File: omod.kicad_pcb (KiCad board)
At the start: 2 copper layers, 147.3 x 97.8 mm, 28 parts, among them P1 Motor_control, P2 Motor_1, P3 Motor_2, Q1 Q_NPN_BCE, Q2 IRF540N, Q3 Q_NPN_BCE, Q4 IRF540N, U1 LM7810ACT

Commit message: ok simulation and removed TVS
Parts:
- removed D5, D7, D9: TVS_30, Diodes_ThroughHole:Diode_DO-35_SOD27_Horizontal_RM10
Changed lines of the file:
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@@
-(kicad_pcb (version 4) (host pcbnew 4.0.3-stable)
+(kicad_pcb (version 4) (host pcbnew 4.0.6)
   (general
-    (links 59)
+    (links 53)
     (no_connects 0)
     (area 12.649999 11.270001 221.209999 110.540001)
@@
     (tracks 250)
     (zones 0)
-    (modules 28)
+    (modules 25)
     (nets 26)
   )
@@
     (pad_to_mask_clearance 0)
     (aux_axis_origin 0 0)
-    (visible_elements 7FFFFFFF)
+    (visible_elements 7FFFEFFF)
     (pcbplotparams
       (layerselection 0x00030_80000001)
@@
   )
   (module Diodes_ThroughHole:Diode_DO-35_SOD27_Horizontal_RM10 placed (layer F.Cu)
-    (at 58.42 73.66 270)
-    (descr "Diode, DO-35,  SOD27, Horizontal, RM 10mm")
-    (tags "Diode, DO-35, SOD27, Horizontal, RM 10mm, 1N4148,")
-    (fp_text reference D5 (at 5.43052 2.53746 270) (layer F.SilkS)
-      (effects (font (size 1 1) (thickness 0.15)))
-    )
-    (fp_text value TVS_30 (at 4.41452 -3.55854 270) (layer F.Fab)
-      (effects (font (size 1 1) (thickness 0.15)))
-    )
-    (fp_line (start 7.36652 -0.00254) (end 8.76352 -0.00254) (layer F.SilkS) (width 0.15))
-    (fp_line (start 2.92152 -0.00254) (end 1.39752 -0.00254) (layer F.SilkS) (width 0.15))
-    (fp_line (start 3.30252 -0.76454) (end 3.30252 0.75946) (layer F.SilkS) (width 0.15))
-    (fp_line (start 3.04852 -0.76454) (end 3.04852 0.75946) (layer F.SilkS) (width 0.15))
-    (fp_line (start 2.79452 -0.00254) (end 2.79452 0.75946) (layer F.SilkS) (width 0.15))
-    (fp_line (start 2.79452 0.75946) (end 7.36652 0.75946) (layer F.SilkS) (width 0.15))
-    (fp_line (start 7.36652 0.75946) (end 7.36652 -0.76454) (layer F.SilkS) (width 0.15))
-    (fp_line (start 7.36652 -0.76454) (end 2.79452 -0.76454) (layer F.SilkS) (width 0.15))
-    (fp_line (start 2.79452 -0.76454) (end 2.79452 -0.00254) (layer F.SilkS) (width 0.15))
-    (pad 2 thru_hole circle (at 10.16052 -0.00254 90) (size 1.69926 1.69926) (drill 0.70104) (layers *.Cu *.Mask F.SilkS)
-      (net 1 GND))
-    (pad 1 thru_hole rect (at 0.00052 -0.00254 90) (size 1.69926 1.69926) (drill 0.70104) (layers *.Cu *.Mask F.SilkS)
-      (net 4 "Net-(D4-Pad1)"))
-    (model Diodes_ThroughHole.3dshapes/Diode_DO-35_SOD27_Horizontal_RM10.wrl
-      (at (xyz 0.2 0 0))
-      (scale (xyz 0.4 0.4 0.4))
-      (rotate (xyz 0 0 180))
-    )
-  )
-  (module Diodes_ThroughHole:Diode_DO-35_SOD27_Horizontal_RM10 placed (layer F.Cu)
     (at 138.43 52.07)
     (descr "Diode, DO-35,  SOD27, Horizontal, RM 10mm")
@@
   )
   (module Diodes_ThroughHole:Diode_DO-35_SOD27_Horizontal_RM10 placed (layer F.Cu)
-    (at 110.49 81.28 180)
-    (descr "Diode, DO-35,  SOD27, Horizontal, RM 10mm")
-    (tags "Diode, DO-35, SOD27, Horizontal, RM 10mm, 1N4148,")
-    (fp_text reference D7 (at 5.43052 2.53746 180) (layer F.SilkS)
-      (effects (font (size 1 1) (thickness 0.15)))
-    )
-    (fp_text value TVS_30 (at 4.41452 -3.55854 180) (layer F.Fab)
-      (effects (font (size 1 1) (thickness 0.15)))
-    )
-    (fp_line (start 7.36652 -0.00254) (end 8.76352 -0.00254) (layer F.SilkS) (width 0.15))
-    (fp_line (start 2.92152 -0.00254) (end 1.39752 -0.00254) (layer F.SilkS) (width 0.15))
-    (fp_line (start 3.30252 -0.76454) (end 3.30252 0.75946) (layer F.SilkS) (width 0.15))
-    (fp_line (start 3.04852 -0.76454) (end 3.04852 0.75946) (layer F.SilkS) (width 0.15))
-    (fp_line (start 2.79452 -0.00254) (end 2.79452 0.75946) (layer F.SilkS) (width 0.15))
-    (fp_line (start 2.79452 0.75946) (end 7.36652 0.75946) (layer F.SilkS) (width 0.15))
-    (fp_line (start 7.36652 0.75946) (end 7.36652 -0.76454) (layer F.SilkS) (width 0.15))
-    (fp_line (start 7.36652 -0.76454) (end 2.79452 -0.76454) (layer F.SilkS) (width 0.15))
-    (fp_line (start 2.79452 -0.76454) (end 2.79452 -0.00254) (layer F.SilkS) (width 0.15))
-    (pad 2 thru_hole circle (at 10.16052 -0.00254) (size 1.69926 1.69926) (drill 0.70104) (layers *.Cu *.Mask F.SilkS)
-      (net 7 "Net-(D7-Pad2)"))
-    (pad 1 thru_hole rect (at 0.00052 -0.00254) (size 1.69926 1.69926) (drill 0.70104) (layers *.Cu *.Mask F.SilkS)
-      (net 8 "Net-(D7-Pad1)"))
-    (model Diodes_ThroughHole.3dshapes/Diode_DO-35_SOD27_Horizontal_RM10.wrl
-      (at (xyz 0.2 0 0))
-      (scale (xyz 0.4 0.4 0.4))
-      (rotate (xyz 0 0 180))
-    )
-  )
-  (module Diodes_ThroughHole:Diode_DO-35_SOD27_Horizontal_RM10 placed (layer F.Cu)
     (at 80.01 67.31 90)
     (descr "Diode, DO-35,  SOD27, Horizontal, RM 10mm")
@@
     (pad 1 thru_hole rect (at 0.00052 -0.00254 270) (size 1.69926 1.69926) (drill 0.70104) (layers *.Cu *.Mask F.SilkS)
       (net 10 "Net-(D8-Pad1)"))
-    (model Diodes_ThroughHole.3dshapes/Diode_DO-35_SOD27_Horizontal_RM10.wrl
-      (at (xyz 0.2 0 0))
-      (scale (xyz 0.4 0.4 0.4))
-      (rotate (xyz 0 0 180))
-    )
-  )
-  (module Diodes_ThroughHole:Diode_DO-35_SOD27_Horizontal_RM10 placed (layer F.Cu)
-    (at 49.53 78.74 180)
-    (descr "Diode, DO-35,  SOD27, Horizontal, RM 10mm")
-    (tags "Diode, DO-35, SOD27, Horizontal, RM 10mm, 1N4148,")
-    (fp_text reference D9 (at 5.43052 2.53746 180) (layer F.SilkS)
-      (effects (font (size 1 1) (thickness 0.15)))
-    )
-    (fp_text value TVS_30 (at 4.41452 -3.55854 180) (layer F.Fab)
-      (effects (font (size 1 1) (thickness 0.15)))
-    )
-    (fp_line (start 7.36652 -0.00254) (end 8.76352 -0.00254) (layer F.SilkS) (width 0.15))
-    (fp_line (start 2.92152 -0.00254) (end 1.39752 -0.00254) (layer F.SilkS) (width 0.15))
-    (fp_line (start 3.30252 -0.76454) (end 3.30252 0.75946) (layer F.SilkS) (width 0.15))
-    (fp_line (start 3.04852 -0.76454) (end 3.04852 0.75946) (layer F.SilkS) (width 0.15))
-    (fp_line (start 2.79452 -0.00254) (end 2.79452 0.75946) (layer F.SilkS) (width 0.15))
-    (fp_line (start 2.79452 0.75946) (end 7.36652 0.75946) (layer F.SilkS) (width 0.15))
-    (fp_line (start 7.36652 0.75946) (end 7.36652 -0.76454) (layer F.SilkS) (width 0.15))
-    (fp_line (start 7.36652 -0.76454) (end 2.79452 -0.76454) (layer F.SilkS) (width 0.15))
-    (fp_line (start 2.79452 -0.76454) (end 2.79452 -0.00254) (layer F.SilkS) (width 0.15))
-    (pad 2 thru_hole circle (at 10.16052 -0.00254) (size 1.69926 1.69926) (drill 0.70104) (layers *.Cu *.Mask F.SilkS)
-      (net 11 "Net-(D9-Pad2)"))
-    (pad 1 thru_hole rect (at 0.00052 -0.00254) (size 1.69926 1.69926) (drill 0.70104) (layers *.Cu *.Mask F.SilkS)
-      (net 12 "Net-(D9-Pad1)"))
     (model Diodes_ThroughHole.3dshapes/Diode_DO-35_SOD27_Horizontal_RM10.wrl
       (at (xyz 0.2 0 0))
@@
   (segment (start 134.62 48.26) (end 134.62306 48.26) (width 1) (layer B.Cu) (net 6))
   (segment (start 144.78052 66.03948) (end 144.78 66.04) (width 1) (layer B.Cu) (net 6))
-  (segment (start 100.32948 81.28254) (end 100.32948 90.16948) (width 2) (layer B.Cu) (net 7) (status 400000))
-  (segment (start 100.32948 90.16948) (end 102.87 92.71) (width 2) (layer B.Cu) (net 7) (status 800000))
+  (segment (start 100.32948 81.28254) (end 100.32948 90.16948) (width 2) (layer B.Cu) (net 7))
+  (segment (start 100.32948 90.16948) (end 102.87 92.71) (width 2) (layer B.Cu) (net 7))
   (segment (start 123.19 54.61) (end 121.92 54.61) (width 2) (layer B.Cu) (net 7))
   (segment (start 104.13746 81.28254) (end 106.68 78.74) (width 2) (layer B.Cu) (net 7))
@@
   (segment (start 124.46 55.88) (end 123.19 54.61) (width 1.9) (layer B.Cu) (net 7))
   (segment (start 123.19 54.61) (end 123.19 54.61) (width 1.9) (layer B.Cu) (net 7))
-  (segment (start 110.48948 81.28254) (end 110.48948 90.09052) (width 2) (layer B.Cu) (net 8) (status 400000))
-  (segment (start 110.48948 90.09052) (end 107.87 92.71) (width 2) (layer B.Cu) (net 8) (status 800000))
+  (segment (start 110.48948 81.28254) (end 110.48948 90.09052) (width 2) (layer B.Cu) (net 8))
+  (segment (start 110.48948 90.09052) (end 107.87 92.71) (width 2) (layer B.Cu) (net 8))
   (segment (start 110.48948 81.28254) (end 110.48948 71.12052) (width 2) (layer B.Cu) (net 8))
   (segment (start 124.46 68.58) (end 124.46 66.04) (width 2) (layer B.Cu) (net 8))
@@
   (segment (start 53.34 57.15) (end 50.8 54.61) (width 2) (layer B.Cu) (net 11))
   (segment (start 53.34 58.42) (end 53.34 57.15) (width 2) (layer B.Cu) (net 11))
-  (segment (start 53.34 66.04) (end 53.34 74.93202) (width 2) (layer B.Cu) (net 12) (status 400000))
-  (segment (start 53.34 74.93202) (end 49.52948 78.74254) (width 2) (layer B.Cu) (net 12) (status 800000))
+  (segment (start 53.34 66.04) (end 53.34 74.93202) (width 2) (layer B.Cu) (net 12))
+  (segment (start 53.34 74.93202) (end 49.52948 78.74254) (width 2) (layer B.Cu) (net 12))
   (segment (start 44.37 92.71) (end 44.37 83.90202) (width 2) (layer B.Cu) (net 12))
   (segment (start 44.37 83.90202) (end 53.34 74.93202) (width 2) (layer B.Cu) (net 12))

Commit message: before new pcb
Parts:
- removed D2: TVS_30, Diodes_ThroughHole:Diode_DO-35_SOD27_Horizontal_RM10
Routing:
- net GND: vias 5 -> 6
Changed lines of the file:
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@@
 (kicad_pcb (version 4) (host pcbnew 4.0.6)
   (general
-    (links 53)
+    (links 51)
     (no_connects 0)
     (area 12.649999 11.270001 221.209999 110.540001)
     (thickness 1.6)
     (drawings 4)
-    (tracks 250)
+    (tracks 253)
     (zones 0)
-    (modules 25)
+    (modules 24)
     (nets 26)
   )
@@
       (scale (xyz 0.3937 0.3937 0.3937))
       (rotate (xyz 0 0 0))
-    )
-  )
-  (module Diodes_ThroughHole:Diode_DO-35_SOD27_Horizontal_RM10 placed (layer F.Cu)
-    (at 132.08 73.66 180)
-    (descr "Diode, DO-35,  SOD27, Horizontal, RM 10mm")
-    (tags "Diode, DO-35, SOD27, Horizontal, RM 10mm, 1N4148,")
-    (fp_text reference D2 (at 5.43052 2.53746 180) (layer F.SilkS)
-      (effects (font (size 1 1) (thickness 0.15)))
-    )
-    (fp_text value TVS_30 (at 4.41452 -3.55854 180) (layer F.Fab)
-      (effects (font (size 1 1) (thickness 0.15)))
-    )
-    (fp_line (start 7.36652 -0.00254) (end 8.76352 -0.00254) (layer F.SilkS) (width 0.15))
-    (fp_line (start 2.92152 -0.00254) (end 1.39752 -0.00254) (layer F.SilkS) (width 0.15))
-    (fp_line (start 3.30252 -0.76454) (end 3.30252 0.75946) (layer F.SilkS) (width 0.15))
-    (fp_line (start 3.04852 -0.76454) (end 3.04852 0.75946) (layer F.SilkS) (width 0.15))
-    (fp_line (start 2.79452 -0.00254) (end 2.79452 0.75946) (layer F.SilkS) (width 0.15))
-    (fp_line (start 2.79452 0.75946) (end 7.36652 0.75946) (layer F.SilkS) (width 0.15))
-    (fp_line (start 7.36652 0.75946) (end 7.36652 -0.76454) (layer F.SilkS) (width 0.15))
-    (fp_line (start 7.36652 -0.76454) (end 2.79452 -0.76454) (layer F.SilkS) (width 0.15))
-    (fp_line (start 2.79452 -0.76454) (end 2.79452 -0.00254) (layer F.SilkS) (width 0.15))
-    (pad 2 thru_hole circle (at 10.16052 -0.00254) (size 1.69926 1.69926) (drill 0.70104) (layers *.Cu *.Mask F.SilkS)
-      (net 1 GND))
-    (pad 1 thru_hole rect (at 0.00052 -0.00254) (size 1.69926 1.69926) (drill 0.70104) (layers *.Cu *.Mask F.SilkS)
-      (net 3 "Net-(D1-Pad1)"))
-    (model Diodes_ThroughHole.3dshapes/Diode_DO-35_SOD27_Horizontal_RM10.wrl
-      (at (xyz 0.2 0 0))
-      (scale (xyz 0.4 0.4 0.4))
-      (rotate (xyz 0 0 180))
     )
   )
@@
   (gr_line (start 160.02 110.49) (end 12.7 110.49) (angle 90) (layer Edge.Cuts) (width 0.1))
   (gr_line (start 160.02 12.7) (end 160.02 110.49) (angle 90) (layer Edge.Cuts) (width 0.1))
+  (via (at 121.91847 73.66153) (size 2.1) (drill 0.8) (layers F.Cu B.Cu) (net 1))
   (segment (start 115.57 81.28) (end 115.57 80.01) (width 2) (layer B.Cu) (net 1))
   (segment (start 142.24 49.53) (end 143.51 50.8) (width 2) (layer B.Cu) (net 1))
@@
   (segment (start 115.57 86.36) (end 115.57 81.28) (width 2) (layer B.Cu) (net 1))
   (segment (start 142.24 48.26) (end 142.24 49.53) (width 2) (layer B.Cu) (net 1))
-  (segment (start 120.64694 72.39) (end 121.91948 73.66254) (width 2) (layer B.Cu) (net 1))
+  (segment (start 120.64694 72.39) (end 121.91847 73.66153) (width 2) (layer B.Cu) (net 1))
+  (segment (start 121.91847 73.66153) (end 121.91948 73.66254) (width 2) (layer B.Cu) (net 1))
   (segment (start 115.57 72.39) (end 120.64694 72.39) (width 2) (layer B.Cu) (net 1))
   (segment (start 113.03 74.93) (end 115.57 72.39) (width 2) (layer B.Cu) (net 1))
@@
   (via (at 102.87 71.12) (size 2.1) (drill 0.8) (layers F.Cu B.Cu) (net 1))
   (segment (start 104.14153 72.39153) (end 102.87 71.12) (width 1.9) (layer F.Cu) (net 1))
-  (segment (start 121.91948 73.66254) (end 120.64847 72.39153) (width 1.9) (layer F.Cu) (net 1))
+  (segment (start 121.91948 73.66254) (end 121.91847 73.66153) (width 1.9) (layer F.Cu) (net 1))
+  (segment (start 121.91847 73.66153) (end 120.64847 72.39153) (width 1.9) (layer F.Cu) (net 1))
   (segment (start 120.64847 72.39153) (end 120.64694 72.39) (width 1.9) (layer F.Cu) (net 1))
   (segment (start 121.91948 73.66254) (end 121.92254 73.66254) (width 1.9) (layer B.Cu) (net 1))

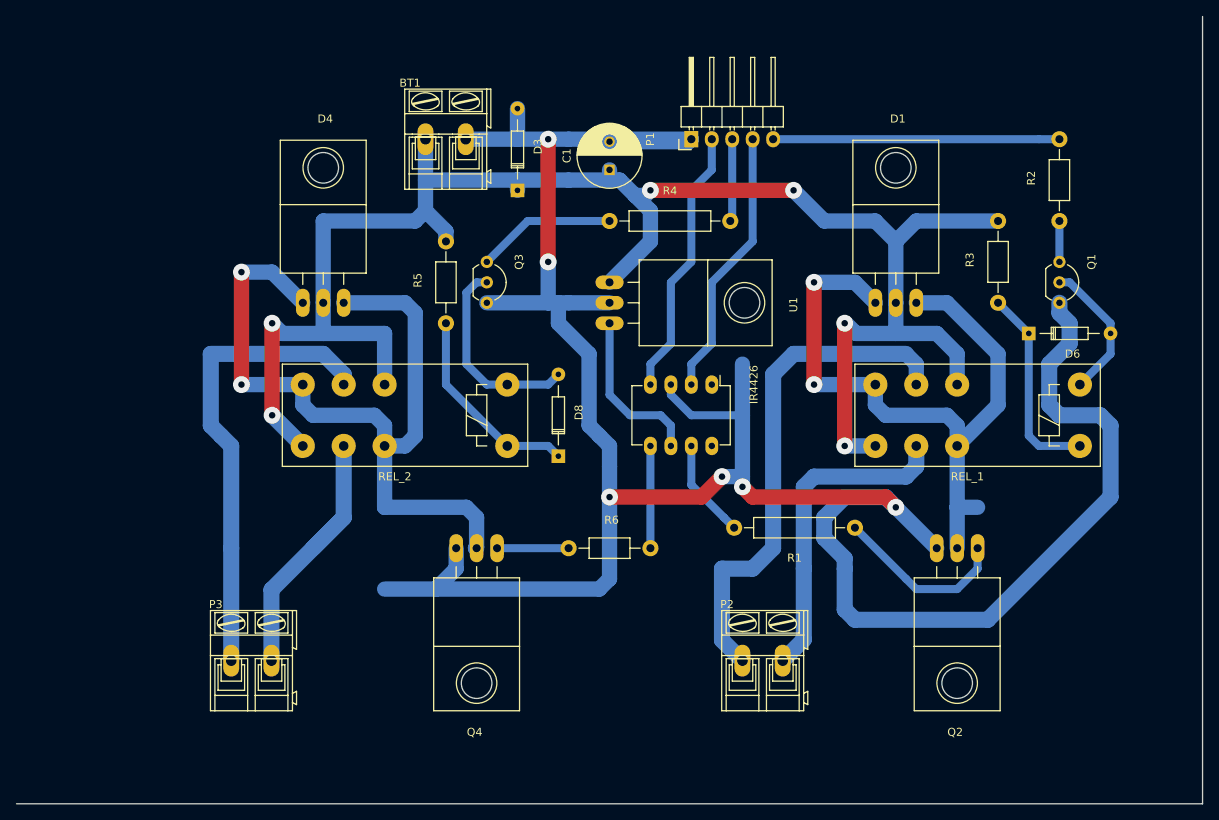
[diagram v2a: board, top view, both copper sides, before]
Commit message: Improve README
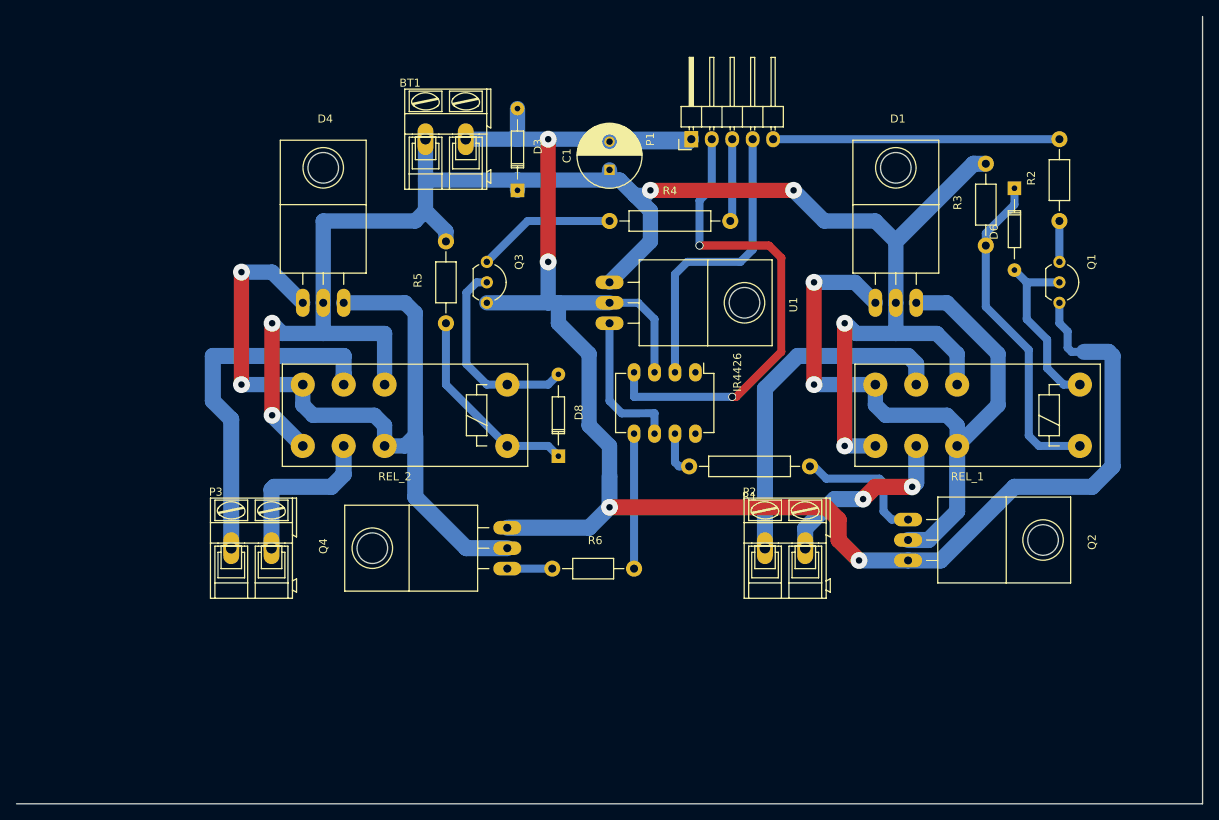
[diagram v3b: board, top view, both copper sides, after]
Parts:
- moved D6 18.1 mm to (136.7, 34.0), turned to -90 degrees
- moved P2 14.2 mm to (105.7, 78.7)
- moved P3 14.0 mm to (39.4, 78.7)
- moved R1 9.45 mm to (111.3, 68.6)
- moved R3 7.27 mm to (133.1, 41.1)
- moved Q2 6.18 mm to (123.4, 77.7), turned to -90 degrees
- moved Q4 3.81 mm to (73.7, 78.7), turned to 90 degrees
- moved R6 3.25 mm to (79.2, 81.3)
- moved IR4426 2.54 mm to (97.0, 56.9)
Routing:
- net GND: track 315.5 -> 230.1 mm, vias 6 -> 4
- net Net-(IR4426-Pad4): track 33.6 -> 60.0 mm, vias 0 -> 2
- net Net-(D7-Pad2): track 63.4 -> 43.3 mm
- net Net-(D7-Pad1): track 40.2 -> 23.2 mm, vias 0 -> 2
- net Net-(D6-Pad1): track 25.0 -> 41.3 mm
- net Net-(D9-Pad1): track 35.8 -> 20.6 mm
- net Net-(D9-Pad2): track 58.0 -> 45.9 mm
- net Net-(IR4426-Pad7): track 12.4 -> 5.91 mm
- net Net-(D6-Pad2): track 17.7 -> 22.8 mm
- net Net-(Q2-Pad1): track 22.0 -> 17.0 mm
- net Net-(IR4426-Pad5): track 12.7 -> 16.8 mm
- net Net-(Q4-Pad1): track 8.89 -> 5.59 mm
- net Net-(IR4426-Pad2): track 33.6 -> 36.8 mm
- net +9V: track 20.6 -> 18.4 mm
- net Net-(D4-Pad1): track 99.7 -> 97.8 mm
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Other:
- net class Default removed
- net class Pow removed
